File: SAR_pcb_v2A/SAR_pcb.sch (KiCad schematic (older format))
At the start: 35 parts, among them J1 Conn_Coaxial_Power, J10 Conn_Coaxial, J2 Conn_Coaxial_Power, J3 Conn_02x10_Top_Bottom, J4 Conn_01x06, J9 Conn_Coaxial, SW1 SW_Push, U2 10B_SAR

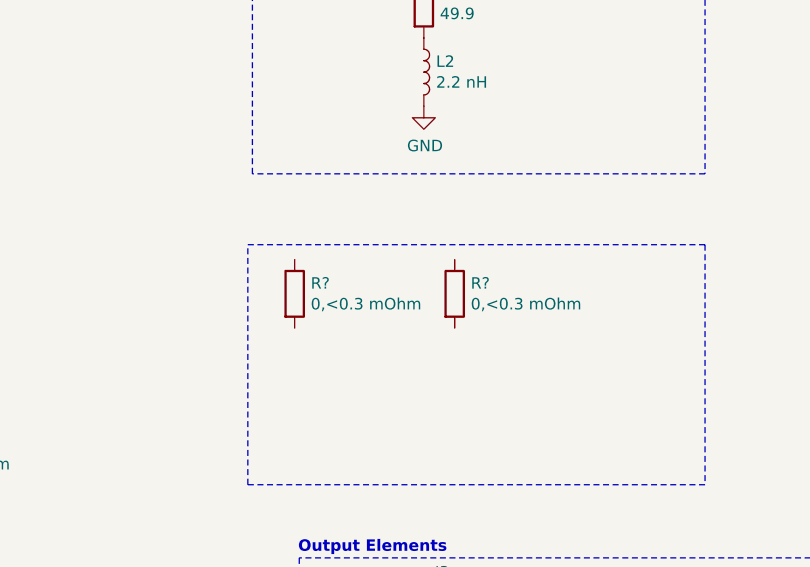
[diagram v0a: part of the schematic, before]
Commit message: Histogram for Chip B1
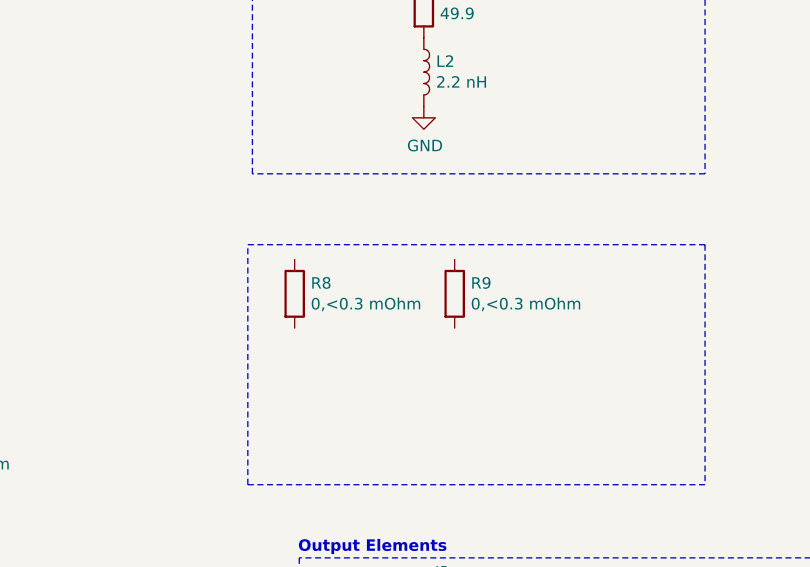
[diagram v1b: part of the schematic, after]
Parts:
- gave numbers to parts that had none: 2
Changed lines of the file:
@@
 	7600 4350 7600 3300
 $Comp
-L Device:R R?
+L Device:R R8
 U 1 1 5F9109D4
 P 7805 3515
-F 0 "R?" H 7875 3561 50  0000 L CNN
+F 0 "R8" H 7875 3561 50  0000 L CNN
 F 1 "0,<0.3 mOhm" H 7875 3470 50  0000 L CNN
 F 2 "Resistor_SMD:R_0603_1608Metric" V 7735 3515 50  0001 C CNN
@@
 $EndComp
 $Comp
-L Device:R R?
+L Device:R R9
 U 1 1 5F913E63
 P 8505 3515
-F 0 "R?" H 8575 3561 50  0000 L CNN
+F 0 "R9" H 8575 3561 50  0000 L CNN
 F 1 "0,<0.3 mOhm" H 8575 3470 50  0000 L CNN
 F 2 "Resistor_SMD:R_0603_1608Metric" V 8435 3515 50  0001 C CNN
